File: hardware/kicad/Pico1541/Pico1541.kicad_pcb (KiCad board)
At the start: 2 copper layers, 100 x 76.2 mm, 62 parts, among them J1 SWD, J2 Serial, J3 Display/Keys, J4 Micro SD Card, J5 5V_EXT, J6 USB_A, J7 OLED/Key_Hat, J8 OLED, J9 DIN-6, Q1 MMBT3904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

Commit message: feat(pio): output SYNC state to GPIO 10 directly from PIO
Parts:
- moved D3 0.05 mm to (120.3, 124.9)
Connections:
- U2 pad 5: +5V -> unconnected-(U2-VP-Pad5)
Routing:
- net Net-(D3-KA): track 0.00 -> 15.3 mm
- net /PLED_N: track 65.1 -> 79.2 mm
- net Net-(D2-GA): track 0.00 -> 9.75 mm
- net Net-(D2-RA): track 0.00 -> 8.71 mm
- net Net-(D2-BA): track 0.00 -> 8.53 mm
- net +5V: track 166.2 -> 160.5 mm, vias 3 -> 2
- net GND: vias 390 -> 388
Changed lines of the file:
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@@
 	(footprint "LED_THT:LED_D5.0mm"
 		(layer "F.Cu")
-		(at 120.225 124.9 180)
+		(at 120.275 124.9 180)
 		(descr "LED, diameter 5.0mm, 2 pins, http://cdn-reichelt.de/documents/datenblatt/A500/LL-504BC2E-009.pdf, generated by kicad-footprint-generator")
 		(tags "LED")
@@
 		)
 		(point
-			(at 118.955 124.9)
+			(at 119.005 124.9)
 			(size 2)
 			(layer "F.Fab")
@@
 			(layers "F.Cu" "F.Mask" "F.Paste")
 			(roundrect_rratio 0.25)
-			(net "+5V")
+			(net "unconnected-(U2-VP-Pad5)")
 			(pinfunction "VP_5")
-			(pintype "passive")
+			(pintype "passive+no_connect")
 		)
 		(pad "6" smd roundrect
@@
 	(footprint "Pico1541-footprints:LED_D5.0mm-4_RGB_CorrectStaggered_Pins"
 		(layer "F.Cu")
-		(at 112.952 125.674 180)
+		(at 112.902 125.674 180)
 		(descr "LED, diameter 5.0mm, 4 pins, WP154A4, https://www.kingbright.com/attachments/file/psearch/000/00/00/L-154A4SUREQBFZGEW(Ver.11A).pdf")
 		(tags "rgb led")
@@
 	)
 	(via
-		(at 111.45 119.85)
-		(size 0.8)
-		(drill 0.4)
-		(layers "F.Cu" "B.Cu")
-		(free yes)
-		(net "GND")
-	)
-	(via
 		(at 163.4 90.75)
 		(size 0.8)
@@
 	)
 	(via
-		(at 116.6 117.75)
-		(size 0.8)
-		(drill 0.4)
-		(layers "F.Cu" "B.Cu")
-		(free yes)
-		(net "GND")
-	)
-	(via
 		(at 104.3 78.81)
 		(size 0.8)
@@
 	)
 	(segment
-		(start 153 75.1)
-		(end 154.3625 75.1)
-		(width 0.5)
-		(layer "F.Cu")
-		(net "+5V")
-	)
-	(segment
 		(start 156.45 89.88)
 		(end 156.45 89.1625)
@@
 	)
 	(via
-		(at 153 75.1)
-		(size 0.8)
-		(drill 0.4)
-		(layers "F.Cu" "B.Cu")
-		(net "+5V")
-	)
-	(via
 		(at 119.25849 64.255283)
 		(size 0.8)
@@
 	)
 	(segment
-		(start 150.35 75.1)
-		(end 153 75.1)
-		(width 0.5)
-		(layer "B.Cu")
-		(net "+5V")
-	)
-	(segment
-		(start 150.35 75.1)
-		(end 149.75 75.1)
-		(width 0.5)
-		(layer "B.Cu")
-		(net "+5V")
-	)
-	(segment
 		(start 147.617874 72.967874)
 		(end 147.617874 63.132126)
@@
 	)
 	(segment
-		(start 149.4 78.65)
-		(end 149.4 75.2)
-		(width 0.5)
-		(layer "B.Cu")
-		(net "+5V")
-	)
-	(segment
-		(start 149.5 75.1)
-		(end 150.35 75.1)
+		(start 147.617874 63.132126)
+		(end 148.4 62.35)
 		(width 0.5)
 		(layer "B.Cu")
@@
 	)
 	(segment
-		(start 147.617874 63.132126)
-		(end 148.4 62.35)
+		(start 149.4 78.65)
+		(end 149.4 74.75)
 		(width 0.5)
 		(layer "B.Cu")
@@
 	)
 	(segment
-		(start 149.75 75.1)
-		(end 147.617874 72.967874)
-		(width 0.5)
-		(layer "B.Cu")
-		(net "+5V")
-	)
-	(segment
 		(start 148.65 60.65)
 		(end 148.4 60.65)
@@
 	)
 	(segment
-		(start 127.202082 58.25)
-		(end 121.352082 64.1)
+		(start 149.4 74.75)
+		(end 147.617874 72.967874)
 		(width 0.5)
 		(layer "B.Cu")
@@
 	)
 	(segment
-		(start 149.4 75.2)
-		(end 149.5 75.1)
+		(start 127.202082 58.25)
+		(end 121.352082 64.1)
 		(width 0.5)
 		(layer "B.Cu")
@@
 	)
 	(segment
-		(start 127.125 83.925)
-		(end 128.55 82.5)
+		(start 120.275 125.325)
+		(end 120.275 124.9)
 		(width 0.25)
 		(layer "F.Cu")
-		(net "/PLED_N")
+		(net "Net-(D3-KA)")
 	)
 	(segment
-		(start 125.991666 83.92)
-		(end 125.996666 83.925)
+		(start 114.4 118.1)
+		(end 115.55 119.25)
 		(width 0.25)
 		(layer "F.Cu")
-		(net "/PLED_N")
+		(net "Net-(D3-KA)")
 	)
 	(segment
-		(start 107.944292 114.305708)
-		(end 118.7 103.55)
+		(start 115.55 119.25)
+		(end 115.55 125.65)
+		(width 0.25)
+		(layer "F.Cu")
+		(net "Net-(D3-KA)")
+	)
+	(segment
+		(start 115.55 125.65)
+		(end 116.9 127)
+		(width 0.25)
+		(layer "F.Cu")
+		(net "Net-(D3-KA)")
+	)
+	(segment
+		(start 118.6 127)
+		(end 120.275 125.325)
+		(width 0.25)
+		(layer "F.Cu")
+		(net "Net-(D3-KA)")
+	)
+	(segment
+		(start 116.9 127)
+		(end 118.6 127)
+		(width 0.25)
+		(layer "F.Cu")
+		(net "Net-(D3-KA)")
+	)
+	(segment
+		(start 114.4 117.25)
+		(end 114.4 118.1)
+		(width 0.25)
+		(layer "F.Cu")
+		(net "Net-(D3-KA)")
+	)
+	(segment
+		(start 117.75 119.25)
+		(end 117.735 119.265)
 		(width 0.25)
 		(layer "F.Cu")
@@
 	)
 	(segment
-		(start 122.979804 83.92)
-		(end 125.991666 83.92)
+		(start 115.35 116.35)
+		(end 117.75 118.75)
 		(width 0.25)
 		(layer "F.Cu")
@@
 	)
 	(segment
-		(start 118.7 103.55)
-		(end 118.7 85.859188)
+		(start 111.35 116.35)
+		(end 115.35 116.35)
 		(width 0.25)
 		(layer "F.Cu")
@@
 	)
 	(segment
-		(start 126.93 64.88)
-		(end 124.31 64.88)
+		(start 125.991666 83.92)
+		(end 125.996666 83.925)
+		(width 0.25)
+		(layer "F.Cu")
+		(net "/PLED_N")
+	)
+	(segment
+		(start 117.735 119.265)
+		(end 117.735 124.9)
 		(width 0.25)
 		(layer "F.Cu")
@@
 	)
 	(segment
-		(start 120.634188 83.925)
-		(end 122.974804 83.925)
+		(start 127.125 83.925)
+		(end 128.55 82.5)
 		(width 0.25)
 		(layer "F.Cu")
@@
 	)
 	(segment
+		(start 117.75 118.75)
+		(end 117.75 119.25)
+		(width 0.25)
+		(layer "F.Cu")
+		(net "/PLED_N")
+	)
+	(segment
+		(start 122.979804 83.92)
+		(end 125.991666 83.92)
+		(width 0.25)
+		(layer "F.Cu")
+		(net "/PLED_N")
+	)
+	(segment
+		(start 126.93 64.88)
+		(end 124.31 64.88)
+		(width 0.25)
+		(layer "F.Cu")
+		(net "/PLED_N")
+	)
+	(segment
+		(start 120.634188 83.925)
+		(end 122.974804 83.925)
+		(width 0.25)
+		(layer "F.Cu")
+		(net "/PLED_N")
+	)
+	(segment
 		(start 118.7 85.859188)
 		(end 120.634188 83.925)
@@
 	)
 	(segment
+		(start 111.35 116.35)
+		(end 111.35 110.9)
+		(width 0.25)
+		(layer "F.Cu")
+		(net "/PLED_N")
+	)
+	(segment
+		(start 118.7 103.55)
+		(end 118.7 85.859188)
+		(width 0.25)
+		(layer "F.Cu")
+		(net "/PLED_N")
+	)
+	(segment
+		(start 111.35 110.9)
+		(end 118.7 103.55)
+		(width 0.25)
+		(layer "F.Cu")
+		(net "/PLED_N")
+	)
+	(segment
 		(start 124.31 54.72)
 		(end 124.305 54.725)
@@
 	)
 	(segment
+		(start 109.15 121.2)
+		(end 108.076 122.274)
+		(width 0.25)
+		(layer "F.Cu")
+		(net "Net-(D2-BA)")
+	)
+	(segment
+		(start 109.15 121.163604)
+		(end 109.15 121.2)
+		(width 0.25)
+		(layer "F.Cu")
+		(net "Net-(D2-BA)")
+	)
+	(segment
+		(start 108.076 122.274)
+		(end 108.076 124.15)
+		(width 0.25)
+		(layer "F.Cu")
+		(net "Net-(D2-BA)")
+	)
+	(segment
+		(start 112 118.313604)
+		(end 109.15 121.163604)
+		(width 0.25)
+		(layer "F.Cu")
+		(net "Net-(D2-BA)")
+	)
+	(segment
+		(start 112 117.25)
+		(end 112 118.313604)
+		(width 0.25)
+		(layer "F.Cu")
+		(net "Net-(D2-BA)")
+	)
+	(segment
+		(start 109.6 125.674)
+		(end 109.6 121.35)
+		(width 0.25)
+		(layer "F.Cu")
+		(net "Net-(D2-GA)")
+	)
+	(segment
+		(start 109.6 121.35)
+		(end 112.8 118.15)
+		(width 0.25)
+		(layer "F.Cu")
+		(net "Net-(D2-GA)")
+	)
+	(segment
+		(start 112.8 118.15)
+		(end 112.8 117.25)
+		(width 0.25)
+		(layer "F.Cu")
+		(net "Net-(D2-GA)")
+	)
+	(segment
+		(start 113.6 124.976)
+		(end 112.902 125.674)
+		(width 0.25)
+		(layer "F.Cu")
+		(net "Net-(D2-RA)")
+	)
+	(segment
+		(start 113.6 117.25)
+		(end 113.6 124.976)
+		(width 0.25)
+		(layer "F.Cu")
+		(net "Net-(D2-RA)")
+	)
+	(segment

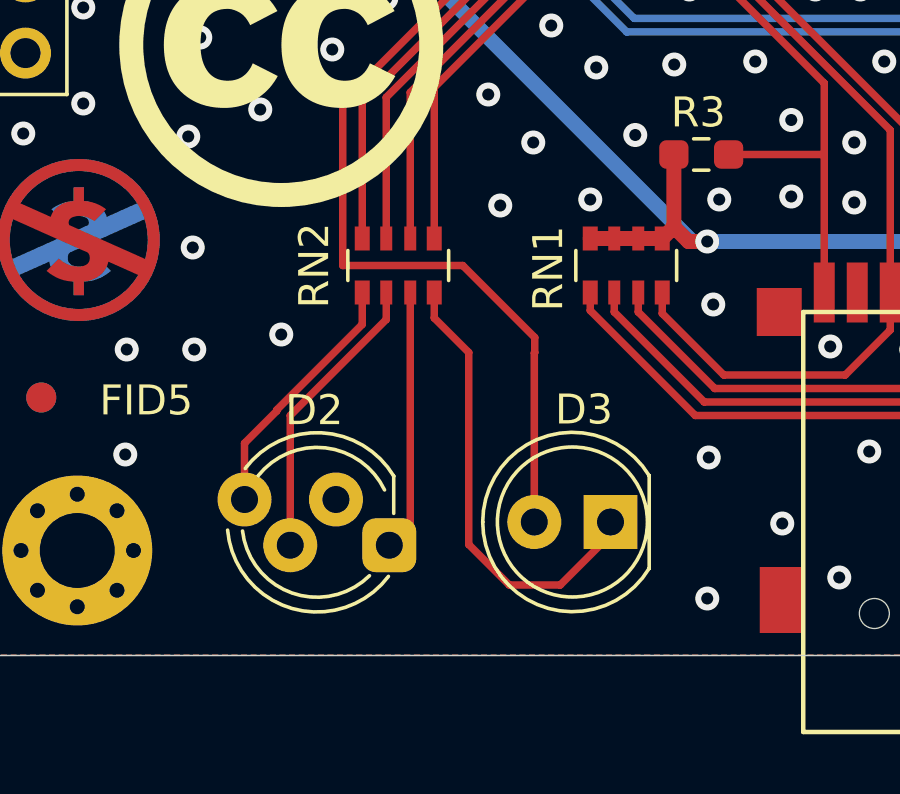
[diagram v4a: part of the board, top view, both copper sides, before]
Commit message: fix(pio): use chained DMA ping-pong and align TrackBuffer to 8192 bytes
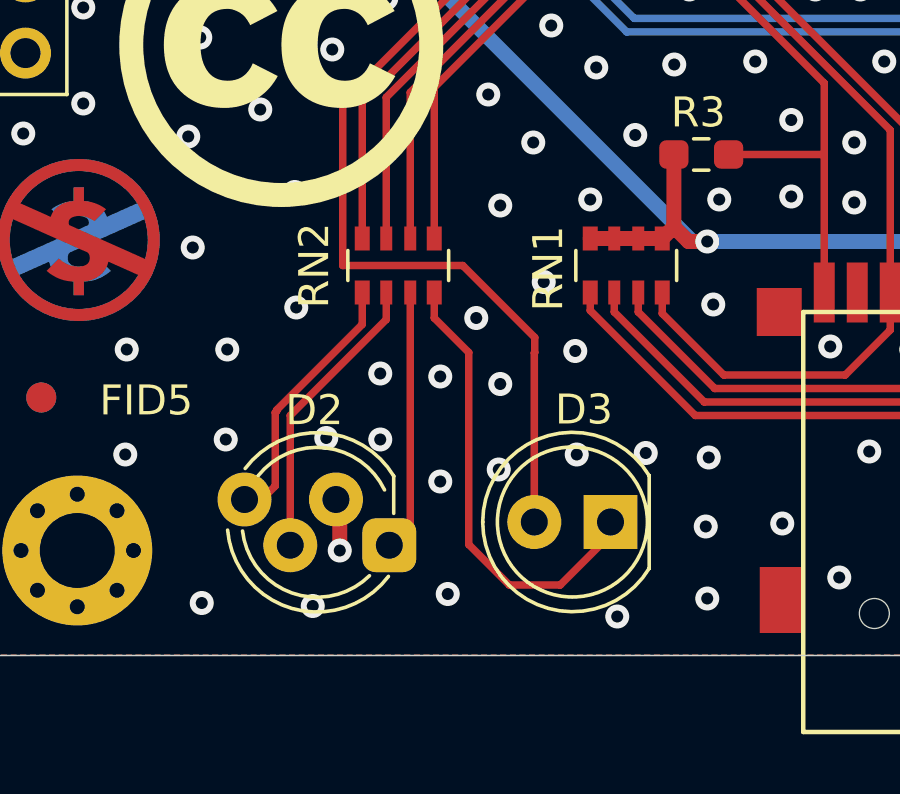
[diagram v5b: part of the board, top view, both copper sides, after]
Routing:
- net GND: track 0.00 -> 1.75 mm, vias 388 -> 408
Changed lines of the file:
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@@
 		(net "/ATN_RX")
 	)
+	(segment
+		(start 111.25 125.85)
+		(end 111.25 124.276)
+		(width 0.5)
+		(layer "F.Cu")
+		(net "GND")
+	)
+	(segment
+		(start 111.25 124.276)
+		(end 111.124 124.15)
+		(width 0.5)
+		(layer "F.Cu")
+		(net "GND")
+	)
 	(via
 		(at 135.4 61.25)
@@
 	)
 	(via
+		(at 112.6 119.95)
+		(size 0.8)
+		(drill 0.4)
+		(layers "F.Cu" "B.Cu")
+		(free yes)
+		(net "GND")
+	)
+	(via
 		(at 109.73 68.53)
 		(size 0.8)
@@
 	)
 	(via
+		(at 115.8 118.1)
+		(size 0.8)
+		(drill 0.4)
+		(layers "F.Cu" "B.Cu")
+		(free yes)
+		(net "GND")
+	)
+	(via
 		(at 144.45 127.85)
 		(size 0.8)
@@
 	)
 	(via
+		(at 114.6 120.05)
+		(size 0.8)
+		(drill 0.4)
+		(layers "F.Cu" "B.Cu")
+		(free yes)
+		(net "GND")
+	)
+	(via
 		(at 138.9 114.85)
 		(size 0.8)
@@
 	)
 	(via
-		(at 109.3 118.65)
+		(at 109.8 117.75)
 		(size 0.8)
 		(drill 0.4)
@@
 	)
 	(via
+		(at 118.05 116.9)
+		(size 0.8)
+		(drill 0.4)
+		(layers "F.Cu" "B.Cu")
+		(free yes)
+		(net "GND")
+	)
+	(via
 		(at 104.25 96.69)
 		(size 0.8)
@@
 	)
 	(via
-		(at 106.4 119.15)
+		(at 107.5 119.15)
 		(size 0.8)
 		(drill 0.4)
@@
 	)
 	(via
+		(at 109.75 113.9)
+		(size 0.8)
+		(drill 0.4)
+		(layers "F.Cu" "B.Cu")
+		(free yes)
+		(net "GND")
+	)
+	(via
 		(at 140.8 124.85)
 		(size 0.8)
@@
 	)
 	(via
+		(at 111.25 125.85)
+		(size 0.8)
+		(drill 0.4)
+		(layers "F.Cu" "B.Cu")
+		(free yes)
+		(net "GND")
+	)
+	(via
 		(at 141.1 73.45)
 		(size 0.8)
@@
 	)
 	(via
+		(at 110.35 127.7)
+		(size 0.8)
+		(drill 0.4)
+		(layers "F.Cu" "B.Cu")
+		(free yes)
+		(net "GND")
+	)
+	(via
 		(at 144.6 117.75)
 		(size 0.8)
@@
 	)
 	(via
+		(at 112.6 122.15)
+		(size 0.8)
+		(drill 0.4)
+		(layers "F.Cu" "B.Cu")
+		(free yes)
+		(net "GND")
+	)
+	(via
 		(at 148.8 106.55)
 		(size 0.8)
@@
 	)
 	(via
+		(at 120.5 128.05)
+		(size 0.8)
+		(drill 0.4)
+		(layers "F.Cu" "B.Cu")
+		(free yes)
+		(net "GND")
+	)
+	(via
 		(at 129.9 54)
 		(size 0.8)
@@
 	)
 	(via
+		(at 106.65 127.6)
+		(size 0.8)
+		(drill 0.4)
+		(layers "F.Cu" "B.Cu")
+		(free yes)
+		(net "GND")
+	)
+	(via
 		(at 150.7 82.76)
 		(size 0.8)
@@
 	)
 	(via
+		(at 116.55 123.15)
+		(size 0.8)
+		(drill 0.4)
+		(layers "F.Cu" "B.Cu")
+		(free yes)
+		(net "GND")
+	)
+	(via
 		(at 156.4 121.25)
 		(size 0.8)
@@
 	)
 	(via
+		(at 110.8 122.1)
+		(size 0.8)
+		(drill 0.4)
+		(layers "F.Cu" "B.Cu")
+		(free yes)
+		(net "GND")
+	)
+	(via
 		(at 159.1 104.95)
 		(size 0.8)
@@
 	)
 	(via
+		(at 116.6 120.3)
+		(size 0.8)
+		(drill 0.4)
+		(layers "F.Cu" "B.Cu")
+		(free yes)
+		(net "GND")
+	)
+	(via
 		(at 136.1 56.4)
 		(size 0.8)
@@
 	)
 	(via
+		(at 123.45 125.05)
+		(size 0.8)
+		(drill 0.4)
+		(layers "F.Cu" "B.Cu")
+		(free yes)
+		(net "GND")
+	)
+	(via
 		(at 117.78 87.73)
 		(size 0.8)
@@
 	)
 	(via
+		(at 119.15 122.65)
+		(size 0.8)
+		(drill 0.4)
+		(layers "F.Cu" "B.Cu")
+		(free yes)
+		(net "GND")
+	)
+	(via
 		(at 127.55 101)
 		(size 0.8)
@@
 	)
 	(via
+		(at 107.45 122.15)
+		(size 0.8)
+		(drill 0.4)
+		(layers "F.Cu" "B.Cu")
+		(free yes)
+		(net "GND")
+	)
+	(via
 		(at 119.6 114.15)
 		(size 0.8)
@@
 	)
 	(via
+		(at 119.1 119.2)
+		(size 0.8)
+		(drill 0.4)
+		(layers "F.Cu" "B.Cu")
+		(free yes)
+		(net "GND")
+	)
+	(via
 		(at 134.1 109)
 		(size 0.8)
@@
 	)
 	(via
+		(at 114.85 127.3)
+		(size 0.8)
+		(drill 0.4)
+		(layers "F.Cu" "B.Cu")
+		(free yes)
+		(net "GND")
+	)
+	(via
+		(at 114.6 123.55)
+		(size 0.8)
+		(drill 0.4)
+		(layers "F.Cu" "B.Cu")
+		(free yes)
+		(net "GND")
+	)
+	(via
 		(at 141 70.15)
 		(size 0.8)
@@
 	)
 	(via
+		(at 121.45 122.6)
+		(size 0.8)
+		(drill 0.4)
+		(layers "F.Cu" "B.Cu")
+		(free yes)
+		(net "GND")
+	)
+	(via
 		(at 129.4 109.55)
 		(size 0.8)
@@
 	)
 	(segment
-		(start 109.15 121.2)
-		(end 108.076 122.274)
+		(start 112 117.25)
+		(end 112 118.313604)
 		(width 0.25)
 		(layer "F.Cu")
@@
 	)
 	(segment
-		(start 109.15 121.163604)
-		(end 109.15 121.2)
+		(start 108.65 124.15)
+		(end 108.076 124.15)
 		(width 0.25)
 		(layer "F.Cu")
@@
 	)
 	(segment
-		(start 108.076 122.274)
-		(end 108.076 124.15)
+		(start 109.15 121.163604)
+		(end 109.15 121.2)
 		(width 0.25)
 		(layer "F.Cu")
@@
 	)
 	(segment
-		(start 112 117.25)
-		(end 112 118.313604)
+		(start 109.1 121.25)
+		(end 109.1 123.7)
+		(width 0.25)
+		(layer "F.Cu")
+		(net "Net-(D2-BA)")
+	)
+	(segment
+		(start 109.1 123.7)
+		(end 108.65 124.15)
+		(width 0.25)
+		(layer "F.Cu")
+		(net "Net-(D2-BA)")
+	)
+	(segment
+		(start 109.15 121.2)
+		(end 109.1 121.25)
 		(width 0.25)
 		(layer "F.Cu")
